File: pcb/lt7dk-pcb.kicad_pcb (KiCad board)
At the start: 2 copper layers, 62 x 84 mm, 53 parts, among them J1 PINHD_1x8_Male, J2 Conn_01x02, J3 PINHD_1x2_Male, J4 PINHD_1x2_Male, J5 PINHD_1x2_Male, J6 PINHD_1x2_Male, SW1 SW_Push, SW2 SW_Push, SW3 SW_Push, SW4 SW_Push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

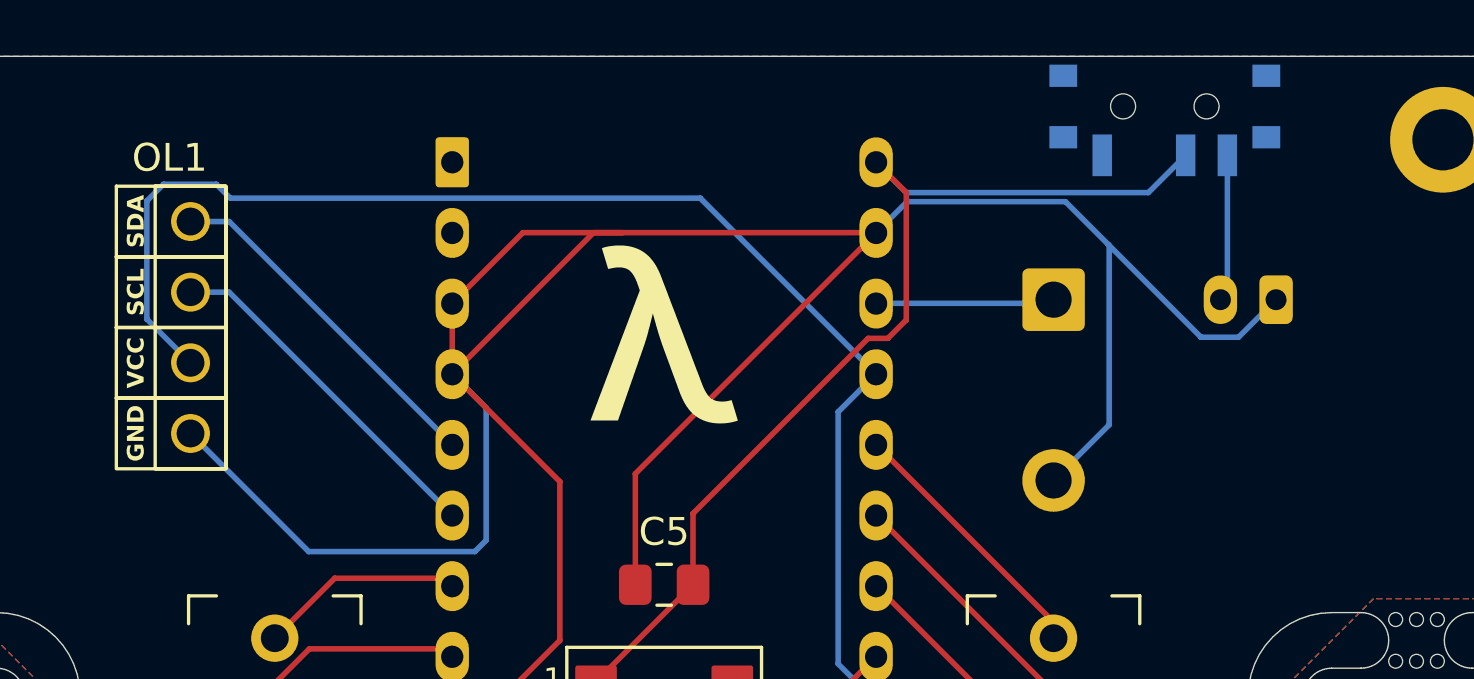
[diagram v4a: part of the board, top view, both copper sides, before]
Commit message: Add PCB order instruction + PTH to add a support for the OLED screen (#2)
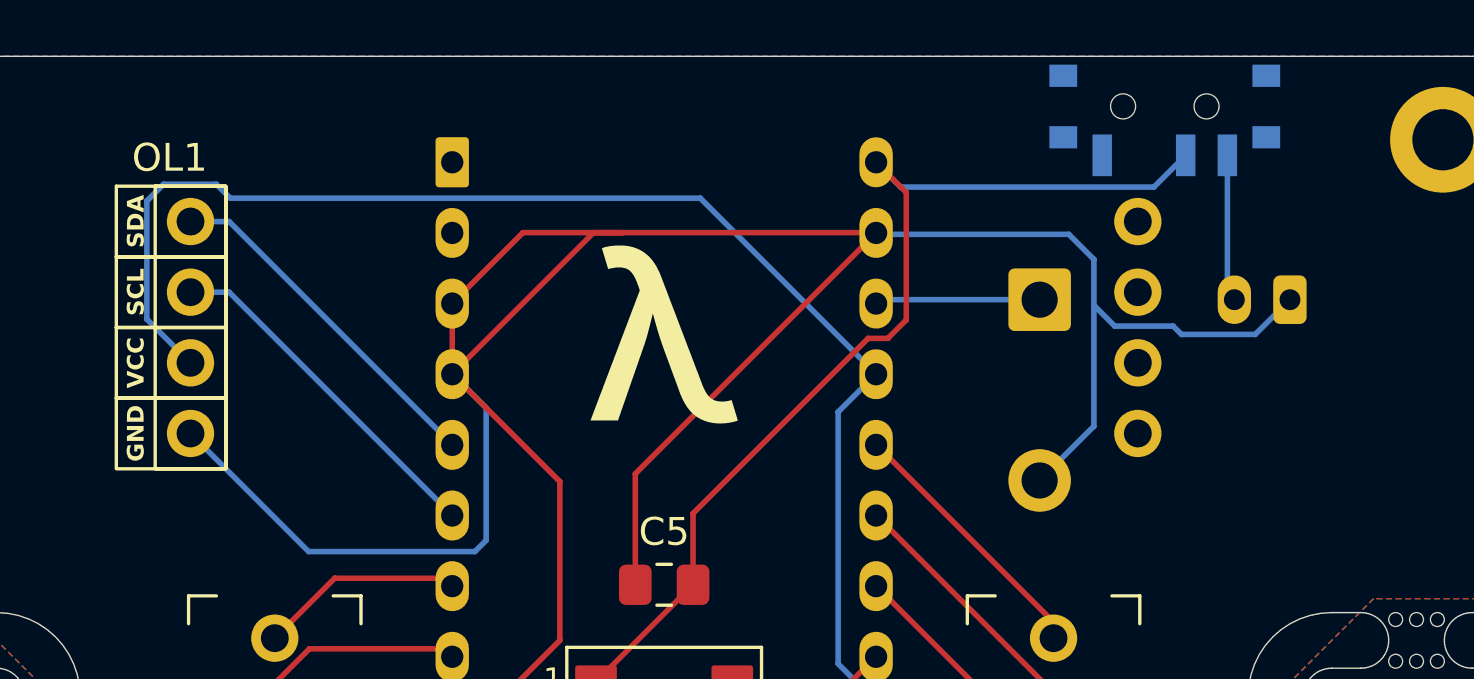
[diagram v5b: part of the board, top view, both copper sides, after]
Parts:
- added J7: PINHD_1x4_Female, Connector_PinSocket_2.54mm:PinSocket_1x04_P2.54mm_Vertical, F.Cu at (88.0, 45.9)
- moved J2 0.50 mm to (93.5, 48.8)
- moved SW8 0.50 mm to (84.5, 52.0)
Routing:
- net GND: track 345.9 -> 344.2 mm
